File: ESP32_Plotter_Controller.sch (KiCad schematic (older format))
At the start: 55 parts, among them J1 ARM JTAG 10pin, J10 Pen Lift, J11 Vselect, J12 X Motor, J13 Y Motor, J14 Neo Pixel LEDs, J15 Pen Direction, J16 Aux Port (I2C), J17 USB_C_Receptacle_USB2.0, J18 E-Stop, J19 Y Limit Switch, J2 Power, J3 5V Aux, J4 Vin Aux, J5 X Limit Switch, J6 Aux Port (SPI), J7 X Limit, J8 Micro_SD_Card_TF-01A, J9 Y Limit, SW1 RESET, SW2 BOOT, U1 ESP32-WROOM-32D, U2 TMC2130, U3 TMC2130, U4 XL1509, U5 CH340C, U6 AMS1117-3.3

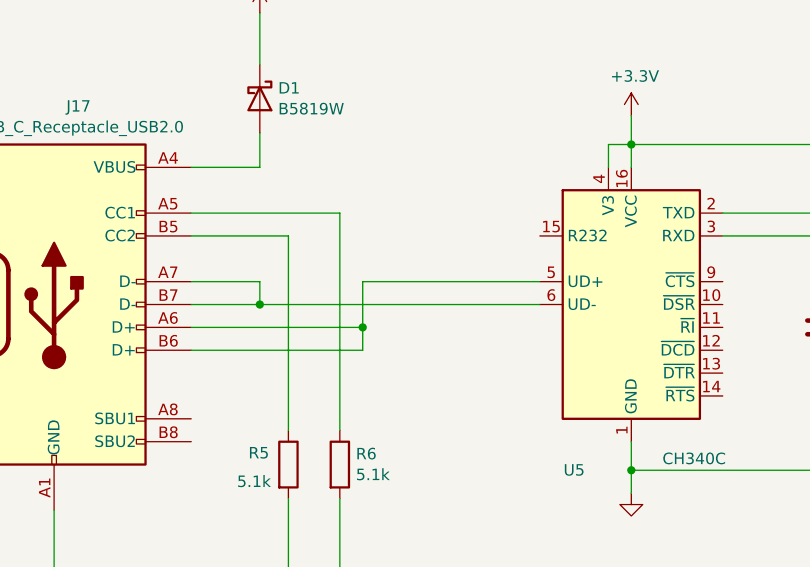
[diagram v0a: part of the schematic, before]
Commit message: Fix USB differential pair routing
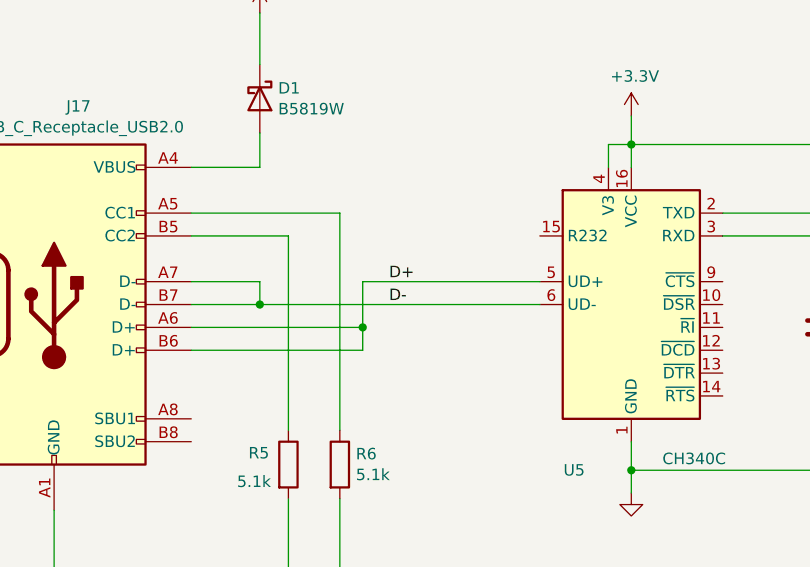
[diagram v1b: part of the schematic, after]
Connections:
- net D+: now reaches J17.A6 (D+), J17.B6 (D+), U5.5 (UD+)
- net D-: now reaches J17.A7 (D-), J17.B7 (D-), U5.6 (UD-)
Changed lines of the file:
@@
 	2395 2010 2395 1960
 Connection ~ 3175 1975
+Text Label 3265 11550 0    50   ~ 0
+D+
+Text Label 3265 11650 0    50   ~ 0
+D-
 $EndSCHEMATC

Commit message: Update LCSC part numbers and production files
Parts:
- C1: LCSC (none) -> C280412
- C11, C12, C13, C14, C4, C5, C8: LCSC (none) -> C42998
- C15: LCSC (none) -> C118989
- C2: LCSC (none) -> C28323
- C3: footprint Capacitor_SMD:CP_Elec_6.3x7.7 -> Capacitor_SMD:CP_Elec_8x10; LCSC (none) -> C242139; LCSC alt (none) -> C413657
- C6, C7: LCSC (none) -> C176688
- D1, D2: LCSC (none) -> C8598
- J1: LCSC (none) -> C92270
- J10: LCSC C10400 (JST PH TH RA) C10400 (JST PH TH RA) C395359 (JST PH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 -> C10400
- J11: LCSC (none) -> C49257
- J12, J13: LCSC C10401 JST PH TH RA -> C10401
- J14, J19, J5: LCSC C10400 (JST PH TH RA) C395359 (JST PH SMT RA) -> C10400
- J15, J18, J3, J4: LCSC C16965 (JST PH TH RA), C47647 (JST PH SMT RA) -> C16965
- J16: LCSC C5662 (JST PH TH RA) C395362 (JST PH SMT RA) -> C5662
- J17: LCSC C165948 (TYPE-C-31-M-12) -> C165948
- J2: LCSC (none) -> C130239
- J6: LCSC C14531 (JST PH TH RA) C519174 (JST PH SMT RA) -> C14531
- J7, J9: LCSC (none) -> C160332
- L1: LCSC (none) -> C439406
- R1, R2: LCSC (none) -> C25201
- R10, R3, R4, R7, R8, R9: LCSC (none) -> C98220
- R5, R6: LCSC (none) -> C269716
- SW1, SW2: LCSC C127509 C118141 (smaller SMT) -> C118141
- U1: LCSC (none) -> C82899
- U2, U3: LCSC (none) -> C27438
- U4: LCSC (none) -> C61063
- U5: LCSC (none) -> C84681
- U6: LCSC (none) -> C351784

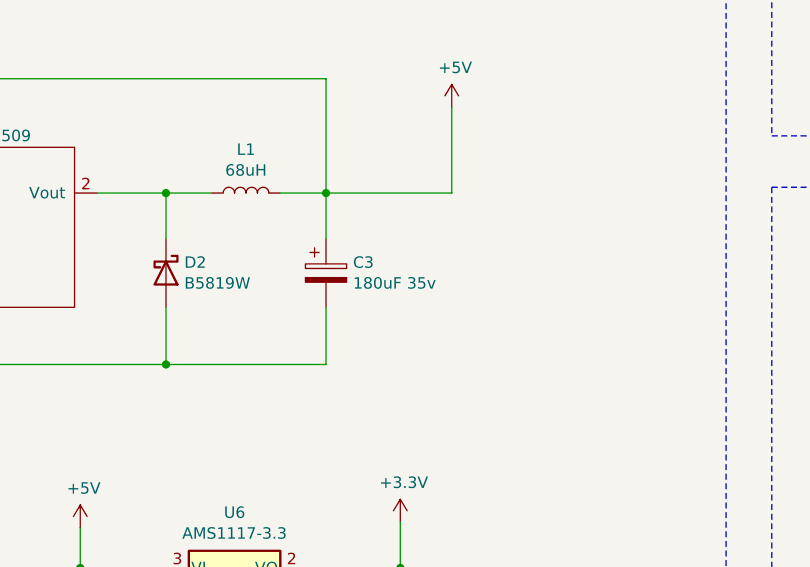
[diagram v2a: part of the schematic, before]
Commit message: Change C3 COUT to 220uF
220uF is more readily available from LCSC and can use a better quality capacitor
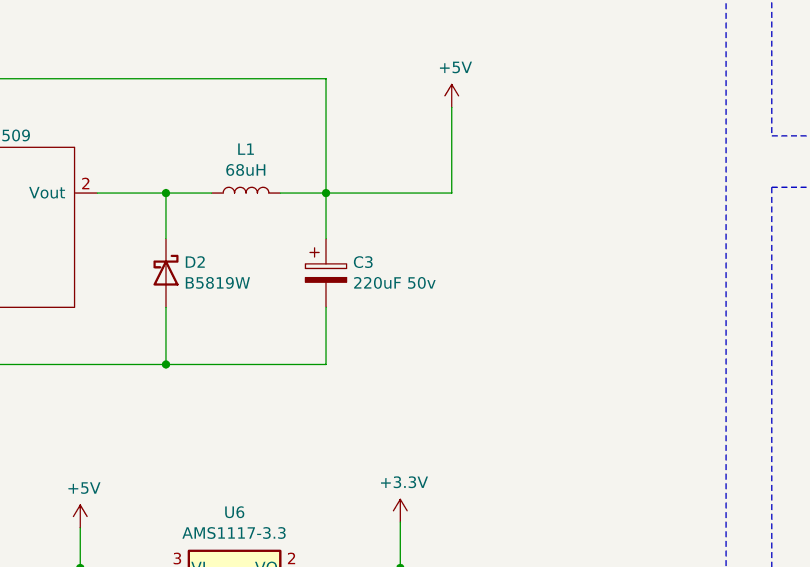
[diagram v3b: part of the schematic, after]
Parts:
- C3: value 180uF 35v -> 220uF 50v; footprint Capacitor_SMD:CP_Elec_8x10 -> Capacitor_SMD:CP_Elec_10x10; LCSC C242139 -> C116211; LCSC alt2 (none) -> C242139
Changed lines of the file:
@@
 P 6700 7160
 F 0 "C3" H 6818 7206 50  0000 L CNN
-F 1 "180uF 35v" H 6818 7115 50  0000 L CNN
-F 2 "Capacitor_SMD:CP_Elec_8x10" H 6738 7010 50  0001 C CNN
+F 1 "220uF 50v" H 6818 7115 50  0000 L CNN
+F 2 "Capacitor_SMD:CP_Elec_10x10" H 6738 7010 50  0001 C CNN
 F 3 "~" H 6700 7160 50  0001 C CNN
-F 4 "C242139" H 6700 7160 50  0001 C CNN "LCSC"
+F 4 "C242139" H 6700 7160 50  0001 C CNN "LCSC alt2"
 F 5 "C413657" H 6700 7160 50  0001 C CNN "LCSC alt"
+F 6 "C116211" H 6700 7160 50  0001 C CNN "LCSC"
 	1    6700 7160
 	1    0    0    -1
